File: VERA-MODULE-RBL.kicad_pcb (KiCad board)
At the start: 4 copper layers, 143 x 162.5 mm, 220 parts, among them J1 CONN_SMD_HEADER_BOX_02x08_Odd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, J2 DS1038-15FBNSiA74-0CC, J3 CONN_DM3AT-SF-PEJM5, J4 DX07S016JA1R1500, J5 PJ-002AH-SMT-TR, J6 CONN_SMD_01x08_Staggered_2.54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, J7 SJ-3523-SMT-TR, Q1 MOSFET-BSS138-SOT-23, Q3 BC817,SOT-23, Q4 BC817,SOT-23, SW1 SPST2P, SW3 SPST2P, U10 W25Q16JVSNIQ, U11 WM8524CGEDT, U12 USBCH340T, U13 AMS1117-3.3, U14 AMS1117-1.2, U15 L7805, U16 74LVC4245APW_118, U17 MAX40200AUK, U18 MAX40200AUK, U19 74LVC4245APW_118, U2 ICE40UP5K-SG48ITR, U23 SN74HCT04DR, U24 SN74LVC00, U25 SN74LVC00, U26 SN74LVC1G07DBVR, U3 74LVC4245APW_118, U4 74LVC4245APW_118, U5 IC74HC00, U6 74LVC4245APW_118, U7 ESP32-S3FN8, U8 74CBTLV3126PW,118, U9 CD4011B, X1 ECS-2033-250-BN, Y1 12MHzC, Y2 40.000Mhz

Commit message: hw: route the board with fastroute, GND and 3V3 as solid planes
- all tracks and vias redone from scratch with fastroute: address and
  data buses first, then the rest; no length-tuning meanders (the 6502
  bus at 1.79 MHz does not need them)
- POWER (3V3) and GND inner layers are solid planes with no tracks;
  every GND and 3V3 SMD pad has its own via to its plane
- U12 (CH340T) on RetroBitLab:SSOP-20_5.3x7.2mm_P0.65mm_Pad0.45, so its
  pads keep 0.2 mm apart instead of exactly the 0.15 mm clearance
- U7 updated from the library with the thermal vias in the exposed pad
- production files and images regenerated
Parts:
- removed D1: BAT43W, Diode_SMD:D_SOD-123
- C1, C11, C15, C16, C17, C18, C20, C23, C24, C55, C57, C58, C66, C67, C68, C9, L1, R2, R34, R6, R64, R66, R69, R7, R70, R71, R72, R75, U23: moved to B.Cu
- U12: footprint Package_SO:SSOP-20_5.3x7.2mm_P0.65mm -> RetroBitLab:SSOP-20_5.3x7.2mm_P0.65mm_Pad0.45
- moved R6 183.3 mm to (270.1, 54.7), turned to 90 degrees
- moved R2 178.6 mm to (267.3, 54.7), turned to 90 degrees
- moved SW3 177.2 mm to (240.8, 90.8)
- moved R33 168.8 mm to (240.8, 96.3)
- moved C64 166.3 mm to (247.0, 110.1), turned to 270 degrees
- moved Y2 159.5 mm to (243.7, 109.8)
- moved C2 157.2 mm to (243.4, 145.5)
- moved JP1 156.2 mm to (263.0, 87.4)
- moved JP3 152.8 mm to (262.9, 83.7)
- moved C61 151.7 mm to (240.8, 94.2), turned to 180 degrees
- moved C65 148.4 mm to (240.7, 110.1), turned to 270 degrees
- moved C9 140.8 mm to (230.5, 138.4), turned to 90 degrees
- moved U23 133.8 mm to (223.3, 150.3), turned to 90 degrees
- moved U5 130.0 mm to (203.0, 112.4), turned to 270 degrees
- moved C1 129.1 mm to (243.4, 138.3), turned to 90 degrees
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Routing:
- net 5V: track 47.1 -> 610.5 mm, vias 2 -> 8
- net Net-(C66-Pad2): track 0.00 -> 238.0 mm, vias 0 -> 2
- net FPGA_CDONE: track 0.00 -> 232.1 mm, vias 0 -> 2
- net ~IRQ: track 0.00 -> 150.8 mm, vias 0 -> 2
- net A15: track 0.00 -> 150.6 mm, vias 0 -> 2
- net A14: track 0.00 -> 140.4 mm, vias 0 -> 2
- net A13: track 0.00 -> 137.2 mm, vias 0 -> 2
- net SPI_MISO: track 0.00 -> 136.7 mm, vias 0 -> 6
- net ~FPGA_RESET: track 0.00 -> 135.8 mm, vias 0 -> 2
- net ~mVCS0: track 0.00 -> 135.8 mm, vias 0 -> 4
- net SPI_SCK: track 0.00 -> 124.4 mm, vias 0 -> 8
- net ESP32_CH340_TXD: track 0.00 -> 124.3 mm, vias 0 -> 2
- net SPI_MOSI: track 0.00 -> 122.9 mm, vias 0 -> 5
- net SPI_SSEL_N: track 0.00 -> 118.4 mm, vias 0 -> 3
- net ESP32_CH340_RXD: track 0.00 -> 112.2 mm, vias 0 -> 2
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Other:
- net class 90R added: clearance 0.15, trace_width 0.2, via_dia 0.8, via_drill 0.4
- net class AddressBus added: clearance 0.15, trace_width 0.2, via_dia 0.6, via_drill 0.4
- net class DataBus added: clearance 0.15, trace_width 0.2, via_dia 0.6, via_drill 0.4
- net class Default: trace_width 0.2 -> 0.23
- net class Power added: clearance 0.15, trace_width 0.3, via_dia 0.8, via_drill 0.4
- board text added: "BOOT0"
- board text added: "RESET"
- board text removed: "VERSATILE EMBEDDED RETRO ADAPTER"

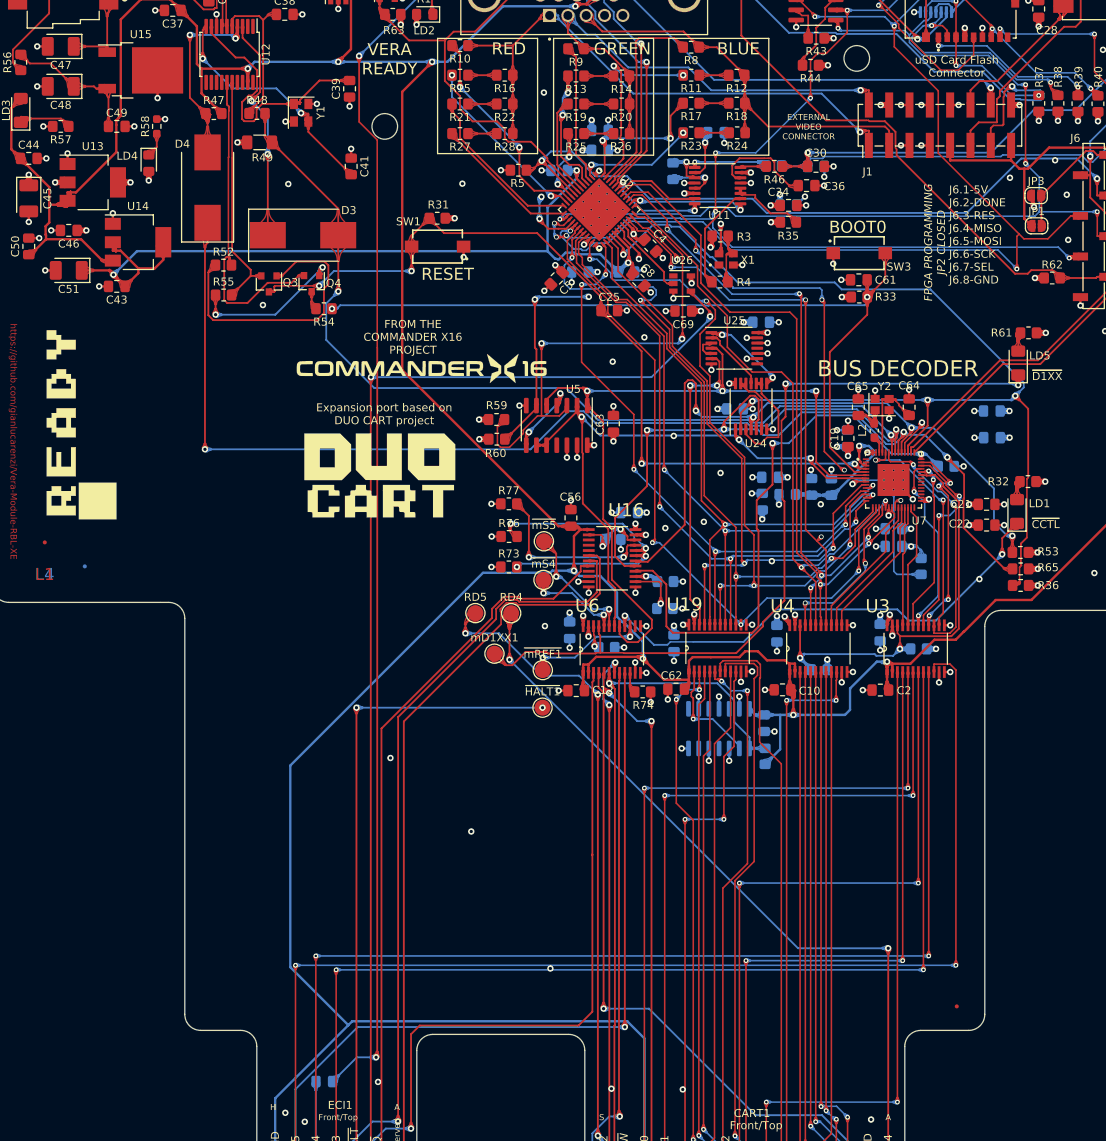
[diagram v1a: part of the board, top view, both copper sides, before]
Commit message: hw: thermal vias under the U13 and U15 tabs
- U15 (L7805, GND tab): 16 vias 0.8/0.4 mm in a 4x4 grid, to the GND
  plane and the B.Cu GND pour
- U13 (AMS1117-3.3, 3V3 tab): 6 vias 0.8/0.4 mm in a 2x3 grid, to the
  3V3 plane
- free vias on the board, the KiCad footprints are unchanged
- zones refilled, a few GND vias moved in pcbnew, production files
  regenerated
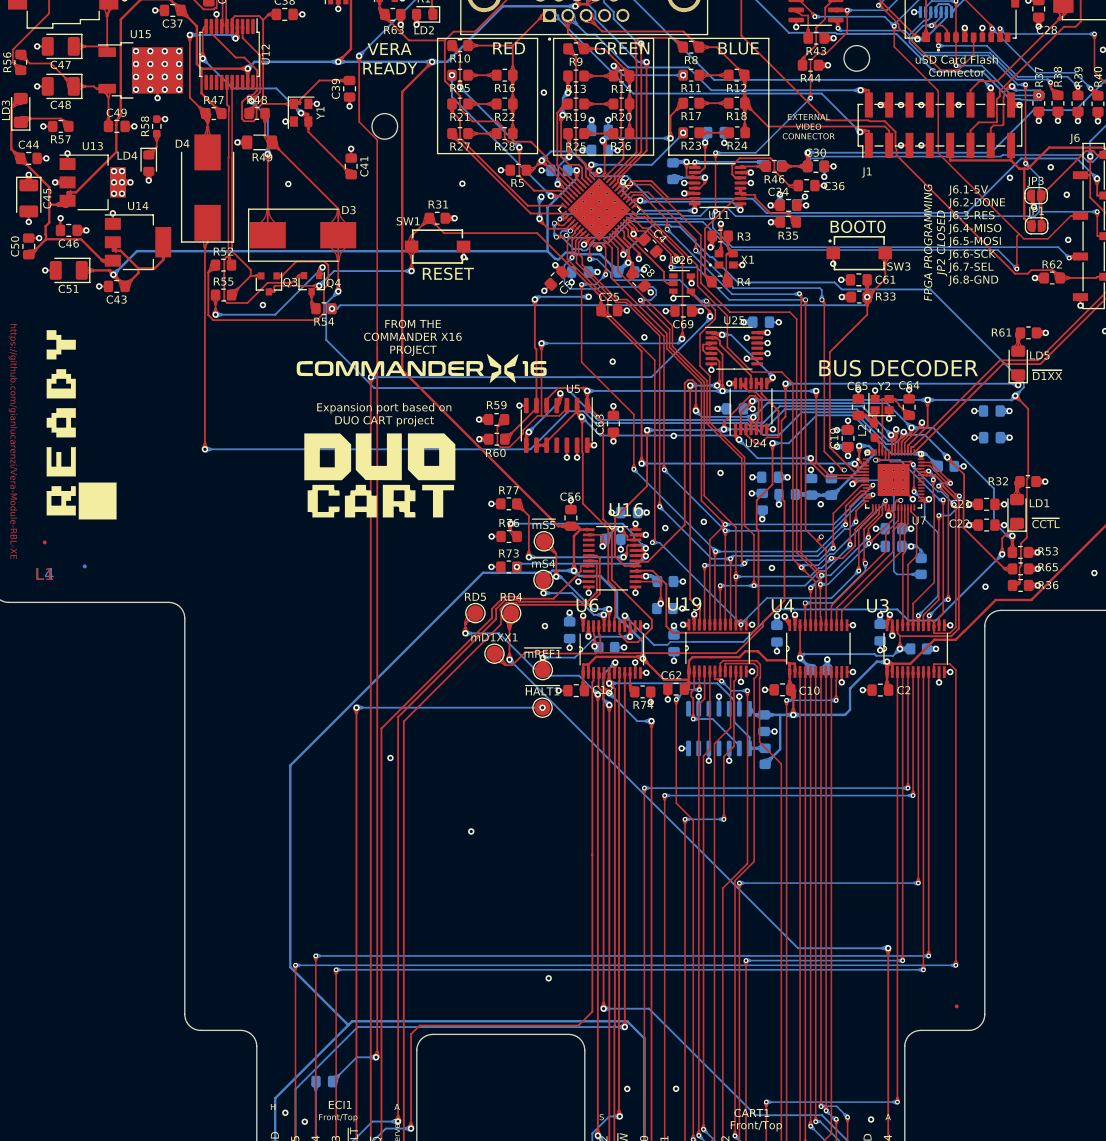
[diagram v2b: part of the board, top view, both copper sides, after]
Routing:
- net GND: track 181.9 -> 182.3 mm, vias 175 -> 190
- net 3V3: vias 90 -> 96

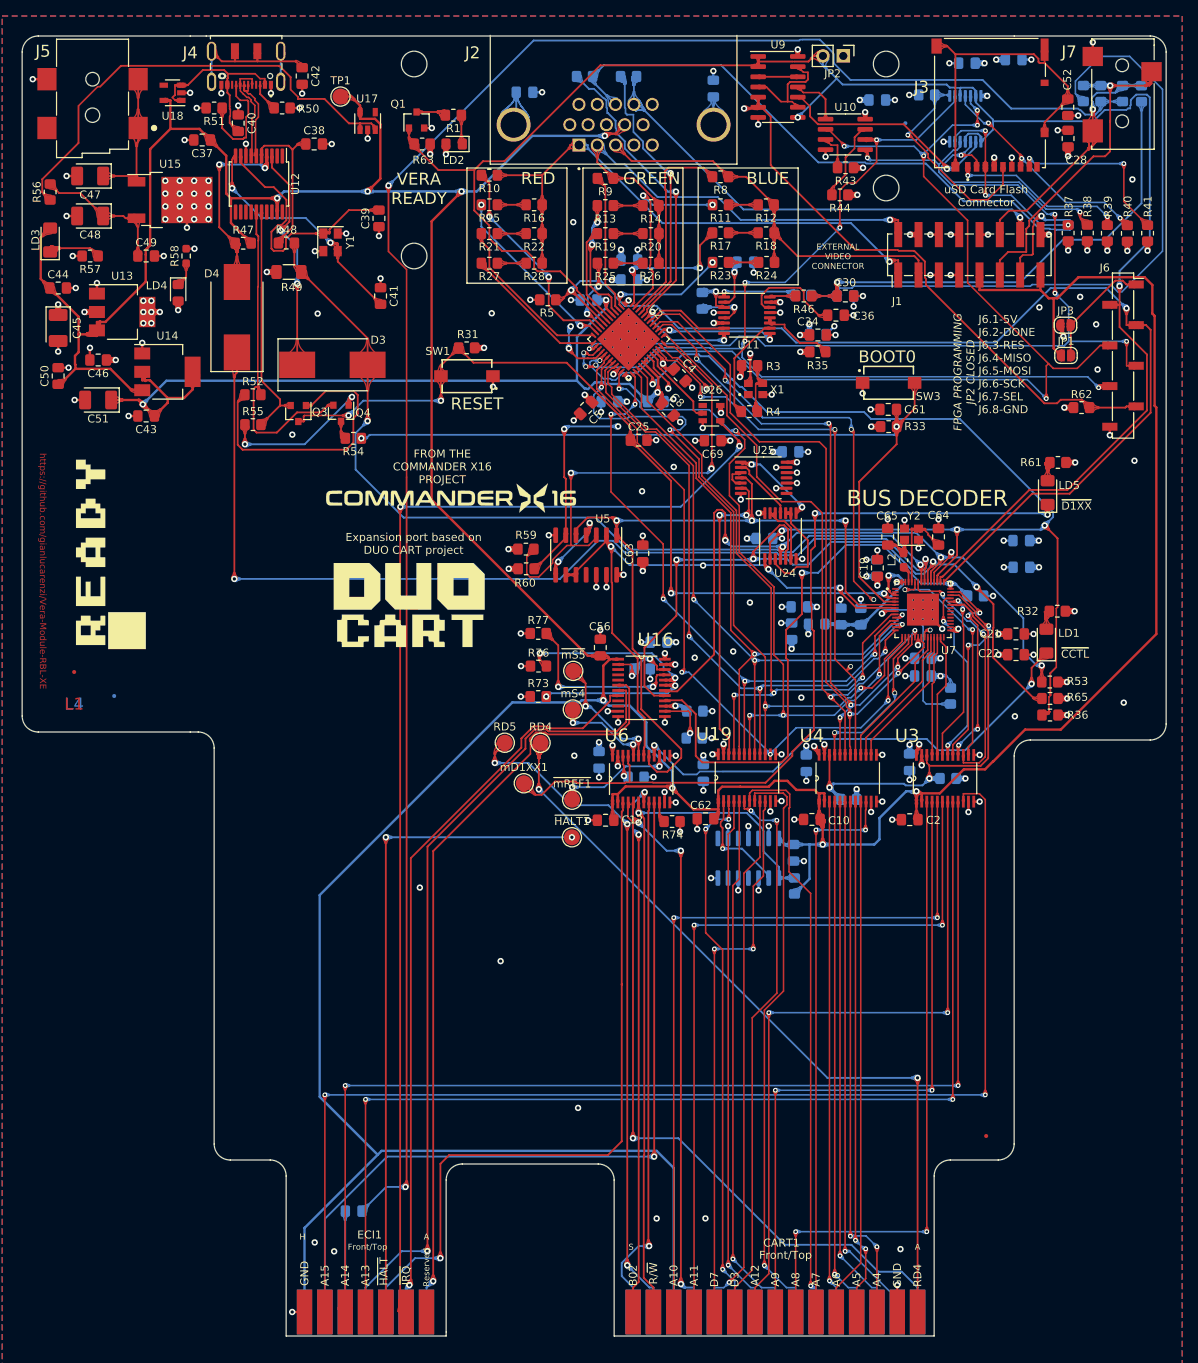
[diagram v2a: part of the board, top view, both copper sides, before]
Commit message: pcb: J7 footprint to jack_3.5_pj313d-smt (PJ-313D, C668608)
Pads 1 sleeve GND, 2 tip AUD1R, 3 ring AUD1L as in the netlist; zones
filled.
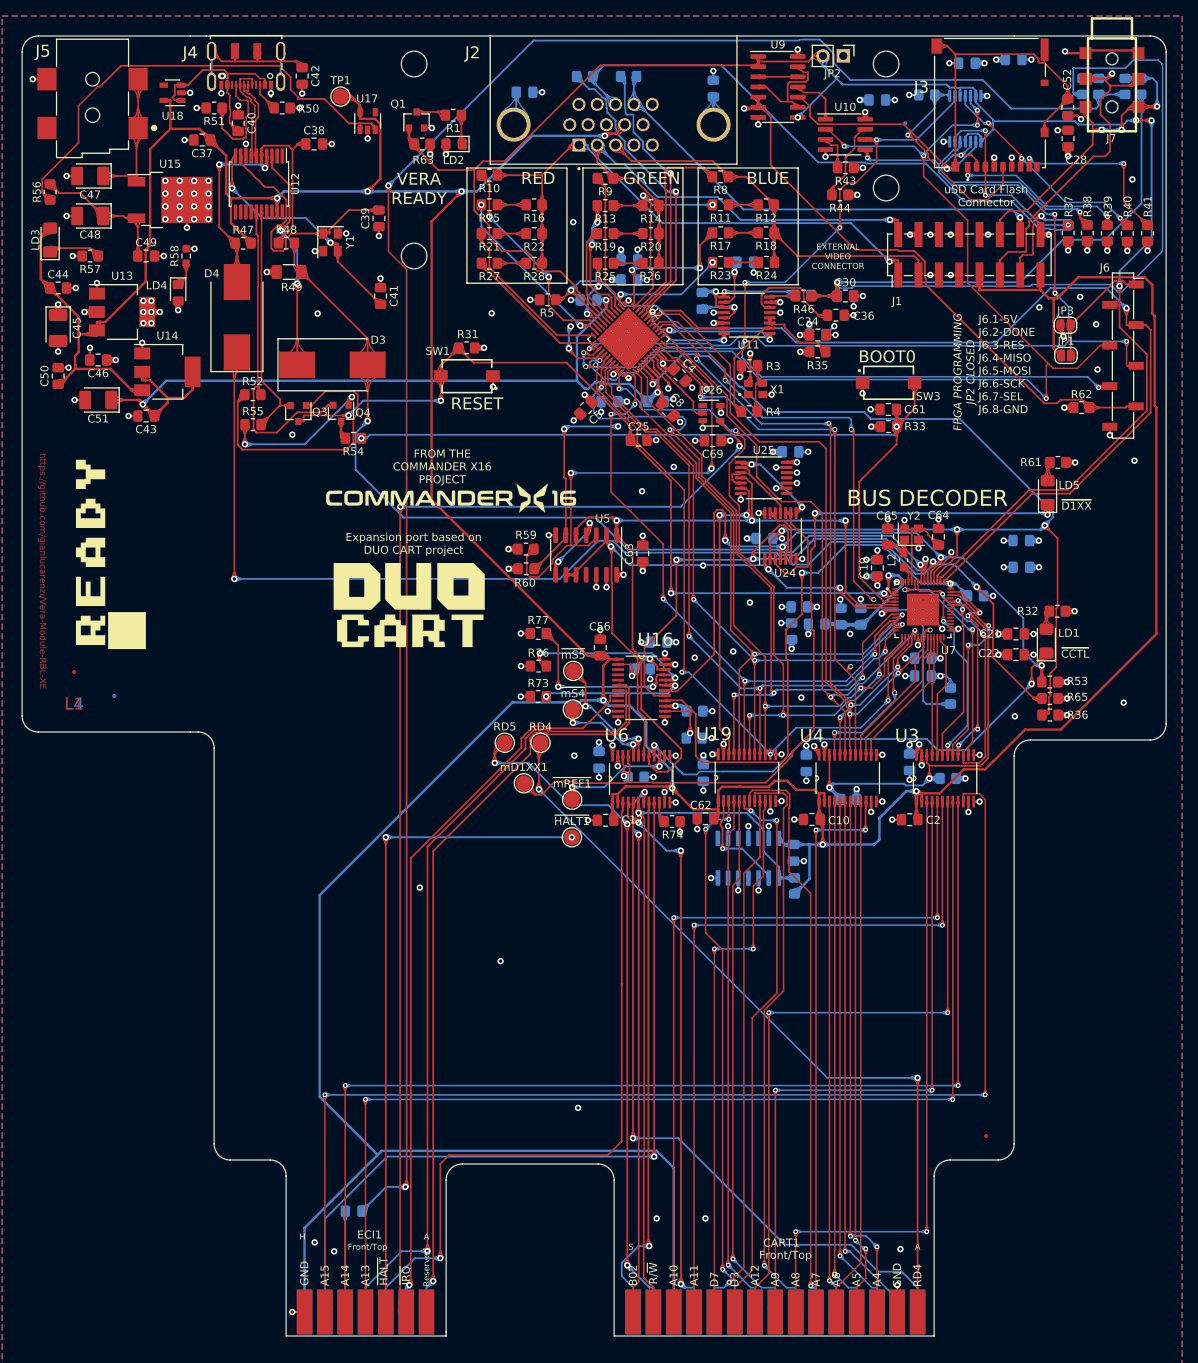
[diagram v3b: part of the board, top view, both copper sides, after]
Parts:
- J7: value SJ-3523-SMT-TR -> PJ-313D; footprint RetroBitLab:CONN_AUDIO_CUI_SJ-3523-SMT-TR -> RetroBitLab:jack_3.5_pj313d-smt
- X1: value ECS-2033-250-BN -> OT3EL89CJI-111YLC-25M
- moved J7 1.65 mm to (268.7, 53.6), turned to 180 degrees
- moved R2 0.94 mm to (267.1, 53.8)
- moved R6 0.94 mm to (270.4, 53.8)
- moved R68 0.92 mm to (272.4, 53.8)
- moved R67 0.89 mm to (265.1, 53.8)
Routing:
- net AUD1R: track 30.1 -> 40.6 mm, vias 1 -> 3
- net GND: track 182.3 -> 190.6 mm
- net AUD1L: track 41.7 -> 47.4 mm
- net FPGA_CDONE: track 232.1 -> 227.9 mm, vias 2 -> 4
- net Net-(C31-Pad1): track 84.6 -> 86.9 mm
- net Net-(C30-Pad1): track 59.7 -> 61.4 mm
